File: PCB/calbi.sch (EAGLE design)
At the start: 15 parts, among them U1 LT3086MPT7

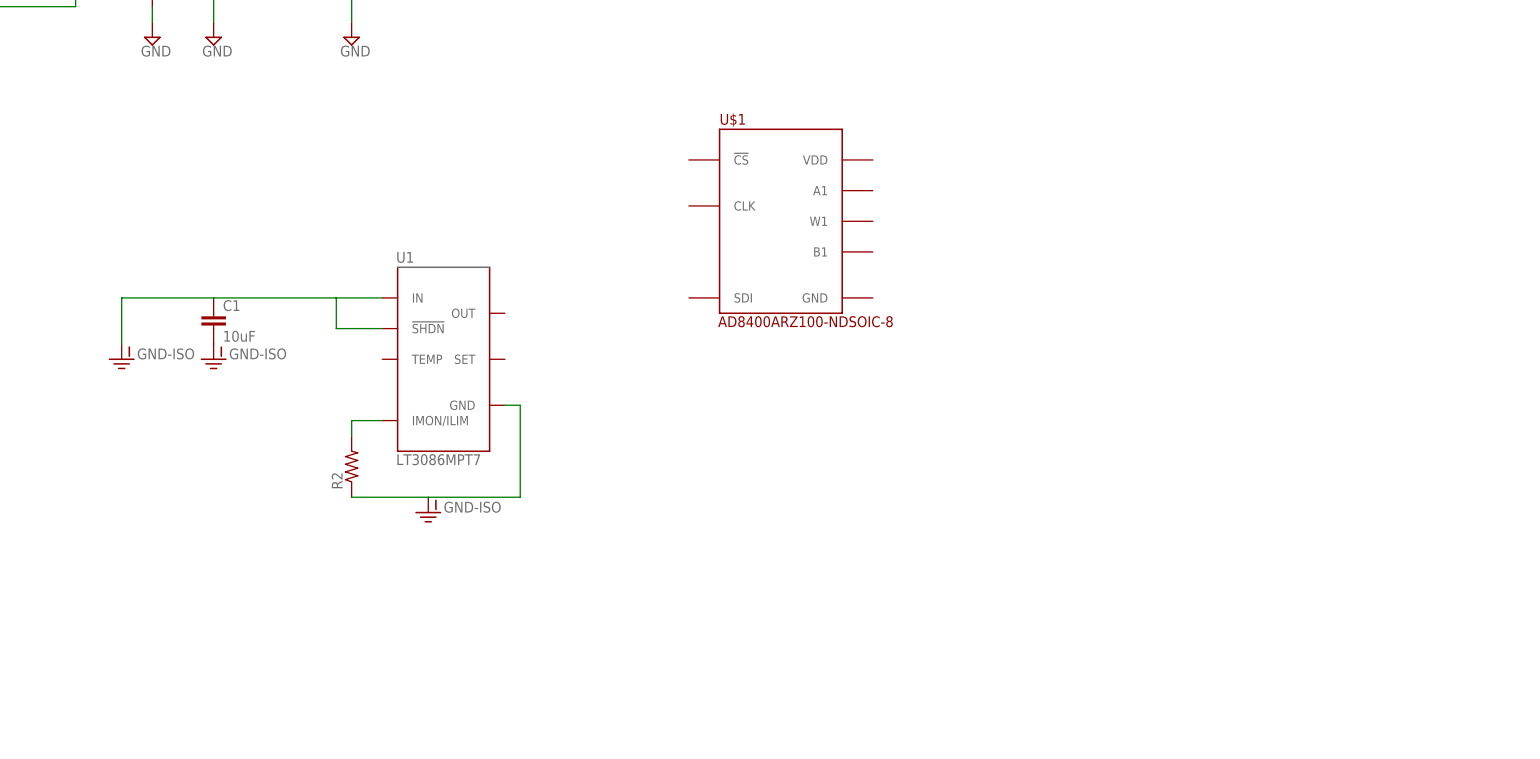
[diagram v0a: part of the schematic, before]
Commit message: Finished schematic for power supply
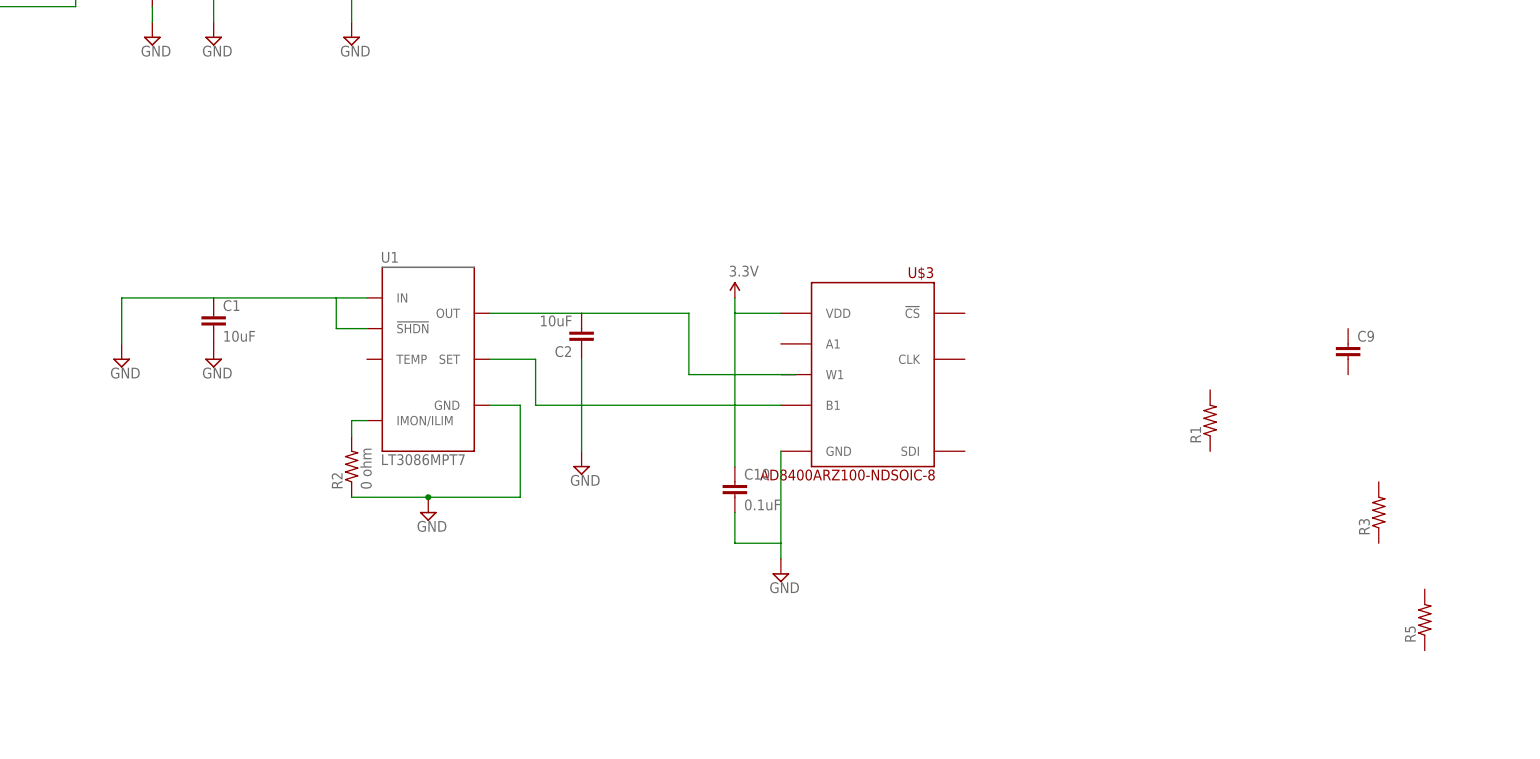
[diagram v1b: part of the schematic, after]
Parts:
- removed U$1: AD8400ARZ100-NDSOIC-8, calbi:AD8400ARZ100-NDSOIC-8
- added C10: 0.1uF, SparkFun-Capacitors:CAP0603-CAP
- added C2: 10uF, SparkFun-Capacitors:CAP0603-CAP
- added C9: (no value), SparkFun-Capacitors:CAP0603-CAP
- added R1, R3, R5: (no value), SparkFun-Passives:RESISTOR0603-RES
- added U$3: AD8400ARZ100-NDSOIC-8, calbi:AD8400ARZ100-NDSOIC-8
- R2: value (none) -> 0 ohm
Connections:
- removed net GND-ISO: C1.1, C1.2, R2.1, U1.!SHDN, U1.GND, U1.IN
- new net N$10: U$3.B1, U1.SET
- new net N$5: C2.2, U1.OUT
- net 3.3V: now also C10.1, U$3.VDD
- net GND: now also C1.1, C1.2, C10.2, C2.1, R2.1, U$3.GND, U1.!SHDN, U1.GND, U1.IN
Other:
- moved on the sheet: U1
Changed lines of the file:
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@@
 <parts>
 <part name="U1" library="calbi" deviceset="LT3086MPT7" device=""/>
-<part name="U$1" library="calbi" deviceset="AD8400ARZ100-ND" device="SOIC-8"/>
 <part name="C1" library="SparkFun-Capacitors" deviceset="CAP" device="0603-CAP" value="10uF"/>
-<part name="R2" library="SparkFun-Passives" deviceset="RESISTOR" device="0603-RES"/>
-<part name="GND-ISO1" library="SparkFun-Aesthetics" deviceset="GND-ISO" device=""/>
-<part name="GND-ISO2" library="SparkFun-Aesthetics" deviceset="GND-ISO" device=""/>
+<part name="R2" library="SparkFun-Passives" deviceset="RESISTOR" device="0603-RES" value="0 ohm"/>
 <part name="U$2" library="calbi" deviceset="AD9835" device=""/>
 <part name="FRAME1" library="SparkFun-Aesthetics" deviceset="FRAME-LEDGER" device=""/>
@@
 <part name="SUPPLY8" library="supply2" deviceset="GND" device=""/>
 <part name="SUPPLY9" library="supply2" deviceset="GND" device=""/>
-<part name="GND-ISO3" library="SparkFun-Aesthetics" deviceset="GND-ISO" device=""/>
 <part name="SUPPLY11" library="supply2" deviceset="GND" device=""/>
 <part name="J$1" library="SparkFun-Connectors" deviceset="SMA_EDGE" device=""/>
 <part name="SUPPLY12" library="supply2" deviceset="GND" device=""/>
+<part name="C9" library="SparkFun-Capacitors" deviceset="CAP" device="0603-CAP"/>
+<part name="R1" library="SparkFun-Passives" deviceset="RESISTOR" device="0603-RES"/>
+<part name="R3" library="SparkFun-Passives" deviceset="RESISTOR" device="0603-RES"/>
+<part name="R5" library="SparkFun-Passives" deviceset="RESISTOR" device="0603-RES"/>
+<part name="SUPPLY1" library="supply2" deviceset="GND" device=""/>
+<part name="SUPPLY10" library="supply2" deviceset="GND" device=""/>
+<part name="SUPPLY13" library="supply2" deviceset="GND" device=""/>
+<part name="U$3" library="calbi" deviceset="AD8400ARZ100-ND" device="SOIC-8"/>
+<part name="C2" library="SparkFun-Capacitors" deviceset="CAP" device="0603-CAP" value="10uF"/>
+<part name="C10" library="SparkFun-Capacitors" deviceset="CAP" device="0603-CAP" value="0.1uF"/>
+<part name="SUPPLY14" library="supply2" deviceset="GND" device=""/>
+<part name="SUPPLY15" library="SparkFun-Aesthetics" deviceset="3.3V" device=""/>
+<part name="SUPPLY16" library="supply2" deviceset="GND" device=""/>
 </parts>
 <sheets>
@@
 </plain>
 <instances>
-<instance part="U1" gate="G$1" x="-35.56" y="129.54"/>
-<instance part="U$1" gate="G$1" x="20.32" y="147.32"/>
+<instance part="U1" gate="G$1" x="-38.1" y="129.54"/>
 <instance part="C1" gate="G$1" x="-73.66" y="134.62"/>
 <instance part="R2" gate="G$1" x="-50.8" y="111.76" rot="R90"/>
-<instance part="GND-ISO1" gate="G$1" x="-73.66" y="129.54"/>
-<instance part="GND-ISO2" gate="G$1" x="-88.9" y="129.54"/>
 <instance part="U$2" gate="G$1" x="-116.84" y="193.04"/>
 <instance part="FRAME1" gate="G$1" x="-223.52" y="-7.62"/>
@@
 <instance part="SUPPLY8" gate="GND" x="-83.82" y="182.88"/>
 <instance part="SUPPLY9" gate="GND" x="-73.66" y="182.88"/>
-<instance part="GND-ISO3" gate="G$1" x="-38.1" y="104.14"/>
 <instance part="SUPPLY11" gate="GND" x="-167.64" y="205.74" rot="R270"/>
 <instance part="J$1" gate="1" x="-58.42" y="198.12" rot="R180"/>
 <instance part="SUPPLY12" gate="GND" x="-50.8" y="182.88"/>
+<instance part="C9" gate="G$1" x="114.3" y="129.54"/>
+<instance part="R1" gate="G$1" x="91.44" y="119.38" rot="R90"/>
+<instance part="R3" gate="G$1" x="119.38" y="104.14" rot="R90"/>
+<instance part="R5" gate="G$1" x="127" y="86.36" rot="R90"/>
+<instance part="SUPPLY1" gate="GND" x="-88.9" y="129.54"/>
+<instance part="SUPPLY10" gate="GND" x="-73.66" y="129.54"/>
+<instance part="SUPPLY13" gate="GND" x="-38.1" y="104.14"/>
+<instance part="U$3" gate="G$1" x="35.56" y="121.92" rot="MR0"/>
+<instance part="C2" gate="G$1" x="-12.7" y="134.62" rot="R180"/>
+<instance part="C10" gate="G$1" x="12.7" y="106.68"/>
+<instance part="SUPPLY14" gate="GND" x="20.32" y="93.98"/>
+<instance part="SUPPLY15" gate="G$1" x="12.7" y="139.7"/>
+<instance part="SUPPLY16" gate="GND" x="-12.7" y="111.76"/>
 </instances>
 <busses>
 </busses>
 <nets>
-<net name="GND-ISO" class="0">
-<segment>
-<pinref part="C1" gate="G$1" pin="2"/>
-<pinref part="GND-ISO1" gate="G$1" pin="GND-ISO"/>
-</segment>
-<segment>
-<pinref part="GND-ISO2" gate="G$1" pin="GND-ISO"/>
-<wire x1="-88.9" y1="132.08" x2="-88.9" y2="139.7" width="0.1524" layer="91"/>
-<pinref part="U1" gate="G$1" pin="IN"/>
-<wire x1="-45.72" y1="139.7" x2="-53.34" y2="139.7" width="0.1524" layer="91"/>
-<pinref part="C1" gate="G$1" pin="1"/>
-<wire x1="-53.34" y1="139.7" x2="-73.66" y2="139.7" width="0.1524" layer="91"/>
-<wire x1="-88.9" y1="139.7" x2="-73.66" y2="139.7" width="0.1524" layer="91"/>
-<pinref part="U1" gate="G$1" pin="!SHDN"/>
-<wire x1="-45.72" y1="134.62" x2="-53.34" y2="134.62" width="0.1524" layer="91"/>
-<wire x1="-53.34" y1="134.62" x2="-53.34" y2="139.7" width="0.1524" layer="91"/>
-</segment>
-<segment>
-<wire x1="-38.1" y1="106.68" x2="-22.86" y2="106.68" width="0.1524" layer="91"/>
-<wire x1="-22.86" y1="106.68" x2="-22.86" y2="121.92" width="0.1524" layer="91"/>
-<pinref part="U1" gate="G$1" pin="GND"/>
-<wire x1="-22.86" y1="121.92" x2="-25.4" y2="121.92" width="0.1524" layer="91"/>
-<pinref part="GND-ISO3" gate="G$1" pin="GND-ISO"/>
-<pinref part="R2" gate="G$1" pin="1"/>
-<wire x1="-50.8" y1="106.68" x2="-38.1" y2="106.68" width="0.1524" layer="91"/>
-</segment>
-</net>
 <net name="3.3V" class="0">
 <segment>
@@
 <pinref part="SUPPLY3" gate="G$1" pin="3.3V"/>
 <wire x1="-142.24" y1="190.5" x2="-152.4" y2="190.5" width="0.1524" layer="91"/>
+</segment>
+<segment>
+<pinref part="U$3" gate="G$1" pin="VDD"/>
+<wire x1="20.32" y1="137.16" x2="12.7" y2="137.16" width="0.1524" layer="91"/>
+<wire x1="12.7" y1="137.16" x2="12.7" y2="111.76" width="0.1524" layer="91"/>
+<pinref part="C10" gate="G$1" pin="1"/>
+<pinref part="SUPPLY15" gate="G$1" pin="3.3V"/>
+<wire x1="12.7" y1="139.7" x2="12.7" y2="137.16" width="0.1524" layer="91"/>
 </segment>
 </net>
@@
 <wire x1="-55.88" y1="203.2" x2="-50.8" y2="203.2" width="0.1524" layer="91"/>
 </segment>
+<segment>
+<wire x1="-88.9" y1="132.08" x2="-88.9" y2="139.7" width="0.1524" layer="91"/>
+<pinref part="U1" gate="G$1" pin="IN"/>
+<wire x1="-48.26" y1="139.7" x2="-53.34" y2="139.7" width="0.1524" layer="91"/>
+<pinref part="C1" gate="G$1" pin="1"/>
+<wire x1="-53.34" y1="139.7" x2="-73.66" y2="139.7" width="0.1524" layer="91"/>
+<wire x1="-88.9" y1="139.7" x2="-73.66" y2="139.7" width="0.1524" layer="91"/>
+<pinref part="U1" gate="G$1" pin="!SHDN"/>
+<wire x1="-48.26" y1="134.62" x2="-53.34" y2="134.62" width="0.1524" layer="91"/>
+<wire x1="-53.34" y1="134.62" x2="-53.34" y2="139.7" width="0.1524" layer="91"/>
+<pinref part="SUPPLY1" gate="GND" pin="GND"/>
+</segment>
+<segment>
+<pinref part="C1" gate="G$1" pin="2"/>
+<pinref part="SUPPLY10" gate="GND" pin="GND"/>
+</segment>
+<segment>
+<wire x1="-50.8" y1="106.68" x2="-38.1" y2="106.68" width="0.1524" layer="91"/>
+<wire x1="-38.1" y1="106.68" x2="-22.86" y2="106.68" width="0.1524" layer="91"/>
+<wire x1="-22.86" y1="106.68" x2="-22.86" y2="121.92" width="0.1524" layer="91"/>
+<pinref part="U1" gate="G$1" pin="GND"/>
+<wire x1="-22.86" y1="121.92" x2="-27.94" y2="121.92" width="0.1524" layer="91"/>
+<pinref part="R2" gate="G$1" pin="1"/>
+<pinref part="SUPPLY13" gate="GND" pin="GND"/>
+<junction x="-38.1" y="106.68"/>
+</segment>
+<segment>
+<pinref part="U$3" gate="G$1" pin="GND"/>
+<wire x1="20.32" y1="114.3" x2="20.32" y2="99.06" width="0.1524" layer="91"/>
+<pinref part="SUPPLY14" gate="GND" pin="GND"/>
+<pinref part="C10" gate="G$1" pin="2"/>
+<wire x1="20.32" y1="99.06" x2="20.32" y2="96.52" width="0.1524" layer="91"/>
+<wire x1="12.7" y1="104.14" x2="12.7" y2="99.06" width="0.1524" layer="91"/>
+<wire x1="12.7" y1="99.06" x2="20.32" y2="99.06" width="0.1524" layer="91"/>
+</segment>
+<segment>
+<pinref part="C2" gate="G$1" pin="1"/>
+<pinref part="SUPPLY16" gate="GND" pin="GND"/>
+<wire x1="-12.7" y1="129.54" x2="-12.7" y2="114.3" width="0.1524" layer="91"/>
+</segment>
 </net>
 <net name="N$4" class="0">
@@
 <segment>
 <pinref part="U1" gate="G$1" pin="IMON/ILIM"/>
-<wire x1="-45.72" y1="119.38" x2="-50.8" y2="119.38" width="0.1524" layer="91"/>
+<wire x1="-48.26" y1="119.38" x2="-50.8" y2="119.38" width="0.1524" layer="91"/>
 <pinref part="R2" gate="G$1" pin="2"/>
 <wire x1="-50.8" y1="119.38" x2="-50.8" y2="116.84" width="0.1524" layer="91"/>
@@
 </segment>
 </net>
+<net name="N$10" class="0">
+<segment>
+<pinref part="U$3" gate="G$1" pin="B1"/>
+<wire x1="20.32" y1="121.92" x2="-20.32" y2="121.92" width="0.1524" layer="91"/>
+<wire x1="-20.32" y1="121.92" x2="-20.32" y2="129.54" width="0.1524" layer="91"/>
+<pinref part="U1" gate="G$1" pin="SET"/>
+<wire x1="-20.32" y1="129.54" x2="-27.94" y2="129.54" width="0.1524" layer="91"/>
+</segment>
+</net>
+<net name="N$5" class="0">
+<segment>
+<pinref part="U1" gate="G$1" pin="OUT"/>
+<pinref part="C2" gate="G$1" pin="2"/>
+<wire x1="-27.94" y1="137.16" x2="-12.7" y2="137.16" width="0.1524" layer="91"/>
+<wire x1="-12.7" y1="137.16" x2="5.08" y2="137.16" width="0.1524" layer="91"/>
+<wire x1="5.08" y1="137.16" x2="5.08" y2="127" width="0.1524" layer="91"/>
+<wire x1="5.08" y1="127" x2="22.86" y2="127" width="0.1524" layer="91"/>
+</segment>
+</net>

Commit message: Finished the schematic
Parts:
- added C11: .1 uF, SparkFun-Capacitors:CAP0603-CAP
- added C12, C13: 1 uF, SparkFun-Capacitors:CAP0603-CAP
- added J1, J2: (no value), SparkFun-Connectors:M023.5MM
- added R7, R9: 2k, SparkFun-Passives:RESISTOR0603-RES
- added R8: 1k, SparkFun-Passives:RESISTOR0603-RES
- added U$1: V_REG_LD1117VXX, SparkFun-PowerIC:V_REG_LD1117VXX
- added U2: 33MHZ-OSCILLATOR, SparkFun-FreqCtrl:33MHZ-OSCILLATOR
- added _1: TEENSY, calbi:TEENSY
- C9: value (none) -> .1 uF
- R1, R5: value (none) -> 1k
- R3: value (none) -> 2k
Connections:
- new net +5V: C10.1, C12.1, C9.1, U$1.IN, U$3.VDD, _1.5V
- new net MOSI: R8.2, U$3.SDI, _1._B2
- new net MOSI3.3: R8.1, U$2.SDATA
- new net N$12: R7.1
- new net N$13: R9.1
- new net N$6: U$2.REFIN, U2.OUT
- new net N$8: C1.1, J1.2, U1.IN
- new net N$9: R3.1
- new net SCLK: R5.2, U$3.CLK, _1._B1
- new net SCLK3.3: R5.1, U$2.SCLK
- new net \CS0: U$3.!CS, _1._B0
- new net \CS1: R1.2, _1._B7
- new net \CS13.3: R1.1, U$2.FSYNC
- new net \SHDN: U1.!SHDN, _1._D0
- net 3.3V: now also C13.1, U$1.OUT, U2.GND, U2.VCC; no longer C10.1, U$3.VDD
- net GND: now also C12.2, C13.2, C9.2, J1.1, J2.2, U$1.GND, _1._GND, _1._GND1; no longer C1.1, U1.!SHDN, U1.IN
- net N$5: now also J2.1, U$3.W1
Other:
- moved on the sheet: C1, C10, C2, C9, R1, R2, R3, R5, U$3, U1
